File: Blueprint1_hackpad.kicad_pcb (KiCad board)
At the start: 2 copper layers, 86 x 66.5 mm, 18 parts, among them SW1 SW_Push, SW2 SW_Push, SW3 SW_Push, SW4 SW_Push, SW5 SW_Push, SW6 SW_Push, SW7 SW_Push, SW8 SW_Push, U1 XIAO-RP2040-DIP

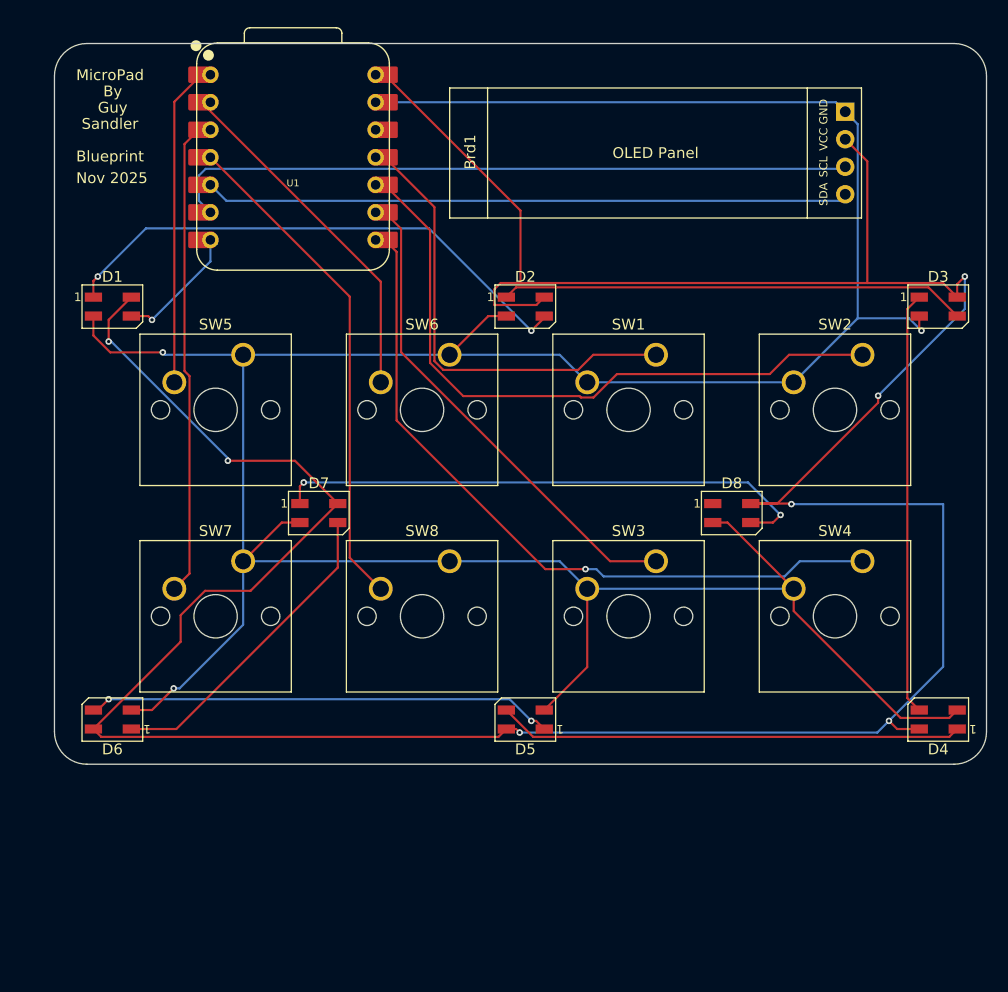
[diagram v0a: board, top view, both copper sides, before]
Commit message: added screw holes
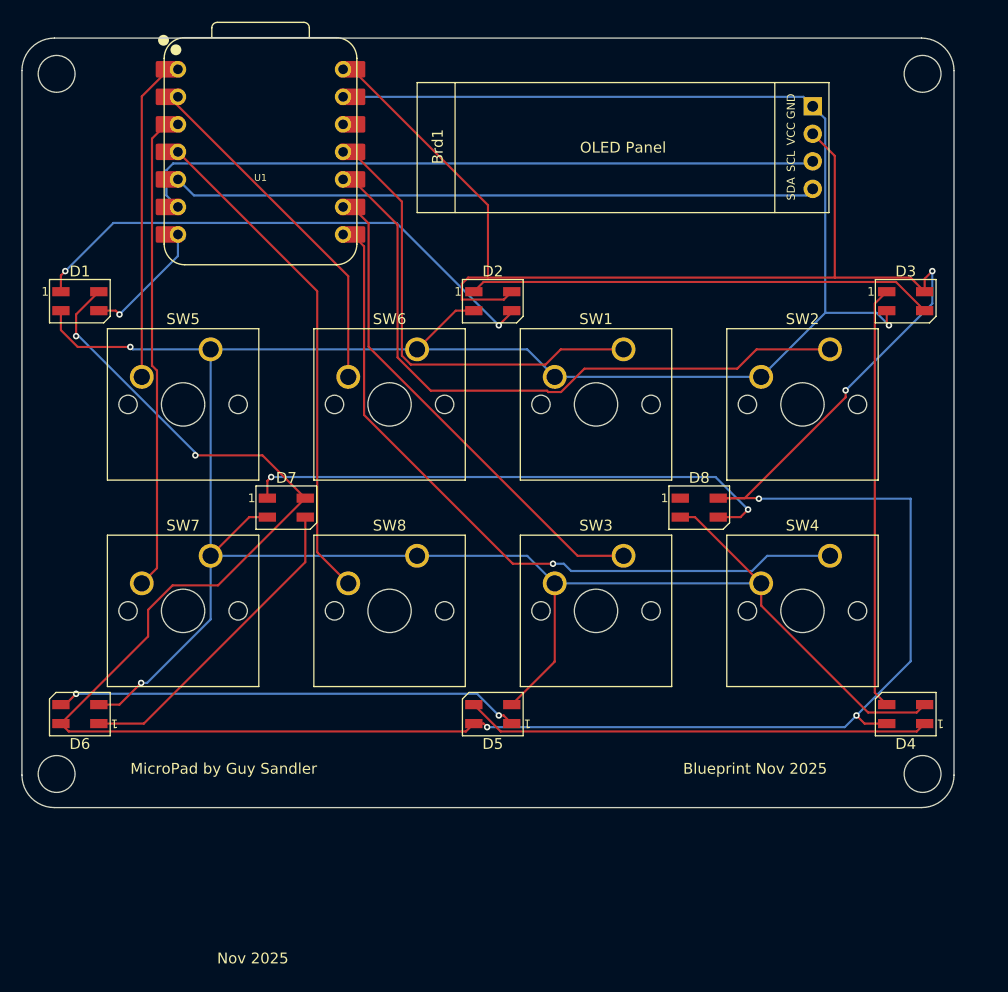
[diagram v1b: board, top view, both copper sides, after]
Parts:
- moved SW3 3.04 mm to (130.5, 127.8)
- moved SW4 3.04 mm to (149.6, 127.8)
- moved SW7 3.04 mm to (92.4, 127.8)
- moved SW8 3.04 mm to (111.5, 127.8)
- moved Brd1 3.04 mm to (111.5, 84.1)
- moved D1 3.04 mm to (80.3, 104.3)
- moved D2 3.04 mm to (118.4, 104.3)
- moved D3 3.04 mm to (156.5, 104.3)
- moved D4 3.04 mm to (156.5, 142.4)
- moved D5 3.04 mm to (118.4, 142.4)
- moved D6 3.04 mm to (80.3, 142.4)
- moved D7 3.04 mm to (99.4, 123.3)
- moved D8 3.04 mm to (137.5, 123.3)
- moved SW1 3.04 mm to (130.5, 108.7)
- moved SW2 3.04 mm to (149.6, 108.7)
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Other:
- board size 86 x 66.5 mm -> 86 x 71 mm
- board text added: "Blueprint Nov 2025"
- board text added: "MicroPad by Guy Sandler"
- board text removed: "Blueprint"
- board text removed: "By"
- board text removed: "Guy"
- board text removed: "MicroPad"
- board text removed: "Sandler"
